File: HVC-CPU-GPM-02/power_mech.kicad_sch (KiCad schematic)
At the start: 19 parts, among them P6 POWER, SW1 RESET, U3 74LS139, U7 74LS368, U8 74LS368

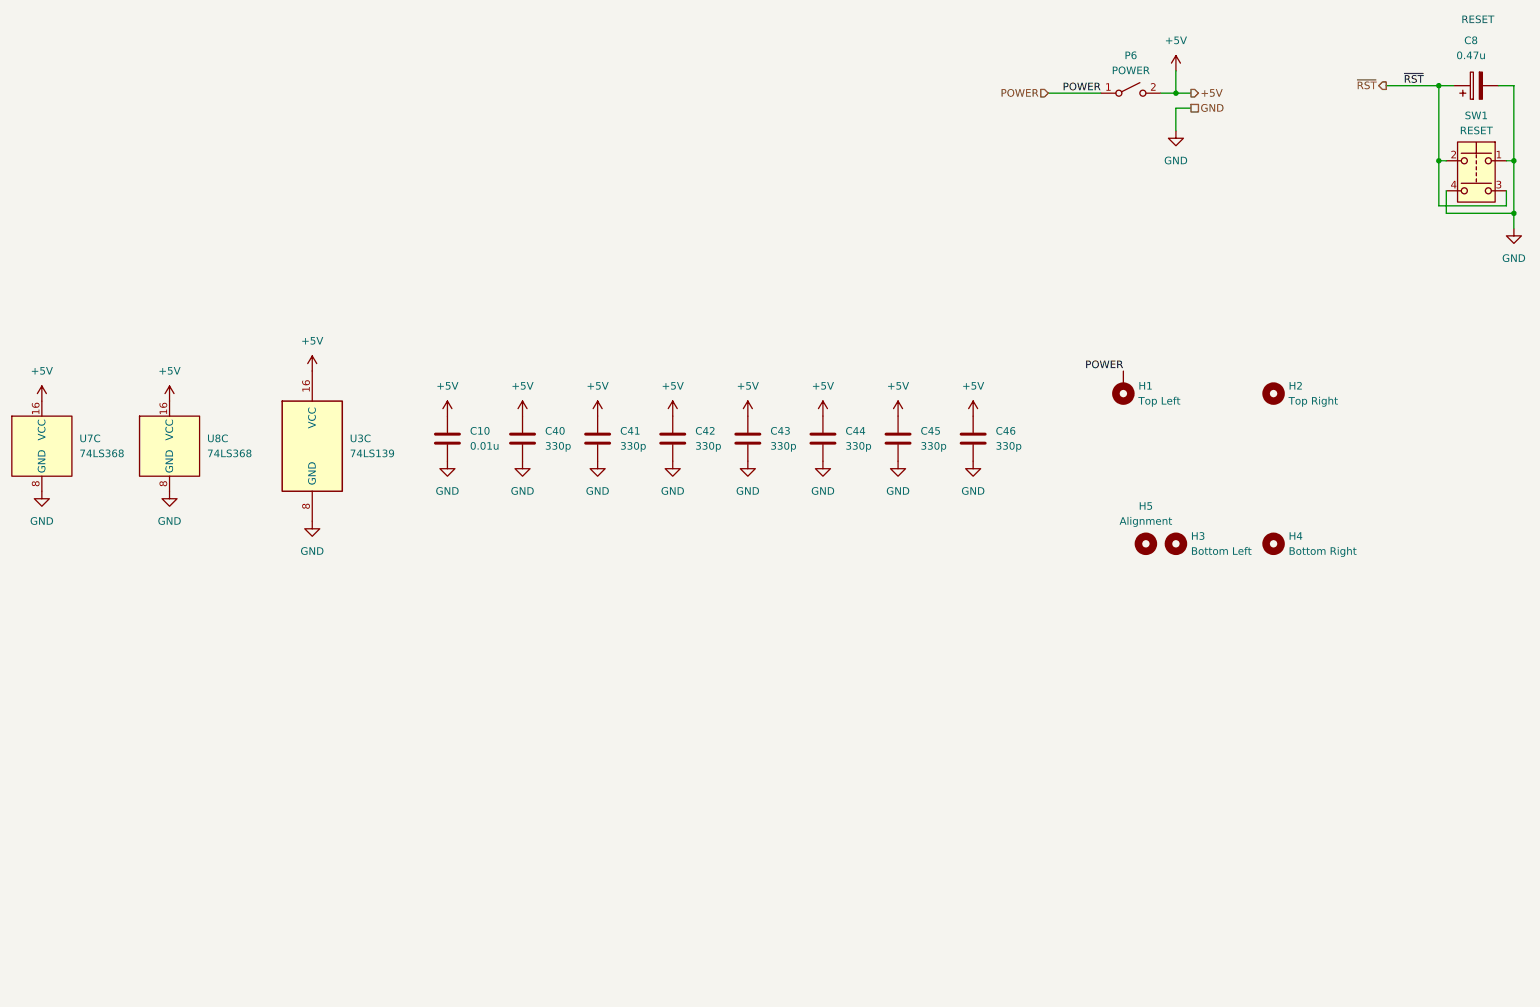
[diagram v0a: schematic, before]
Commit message: Change symbols to functional layout instead of pin map layout Add technical page to store pinouts Organize and compact root page
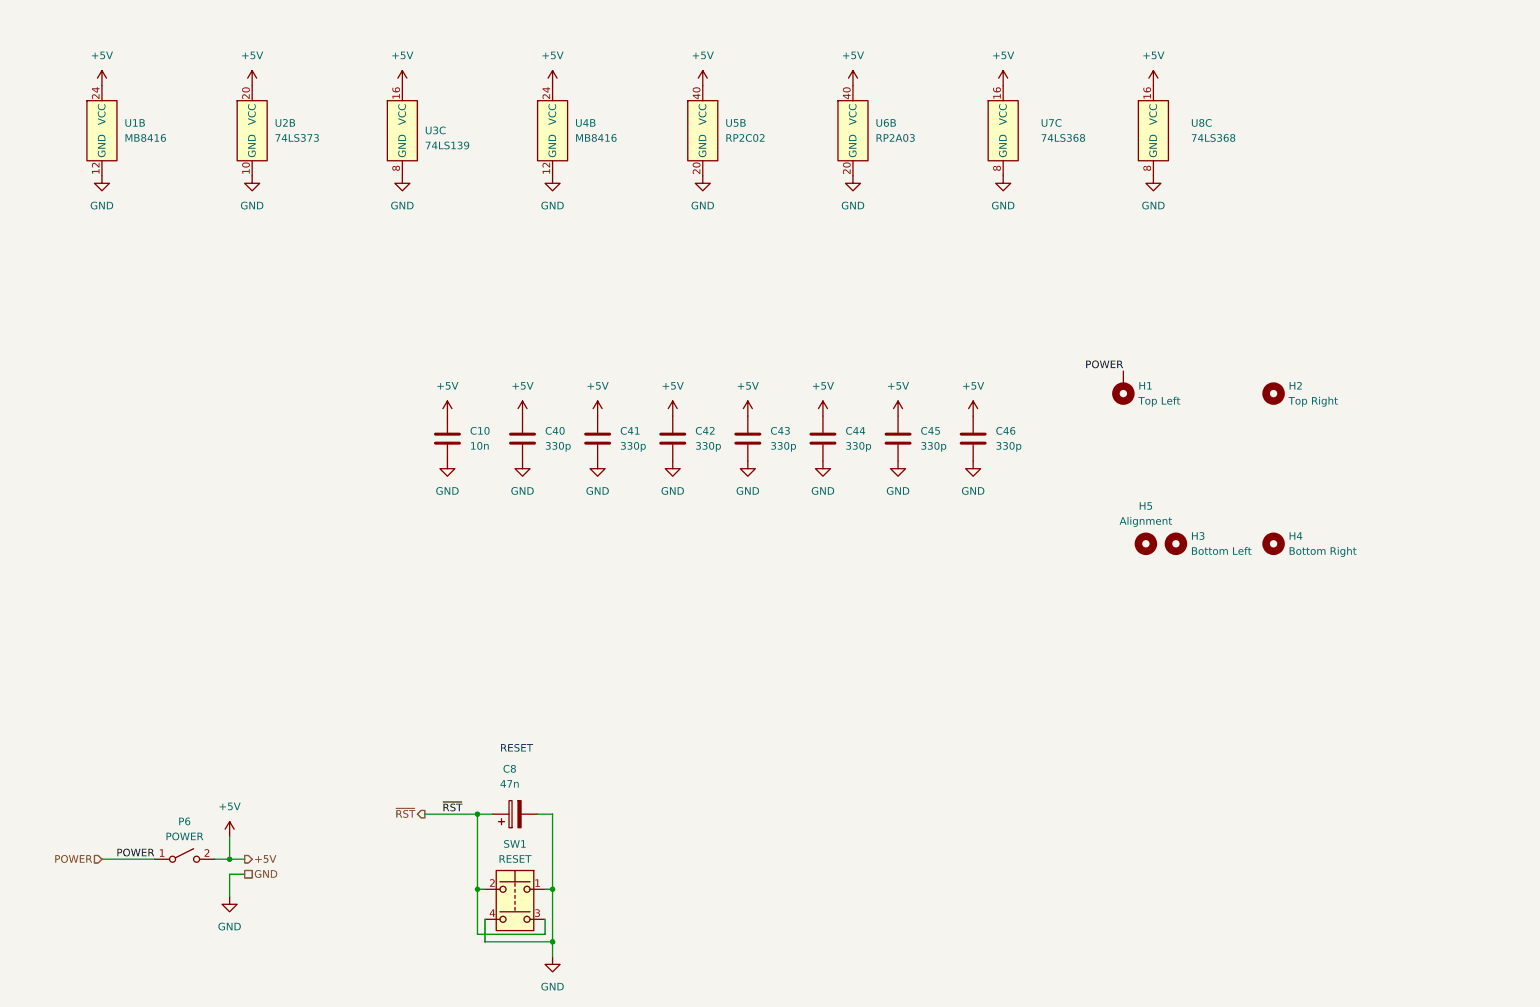
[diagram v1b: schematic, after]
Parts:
- added U1, U4: MB8416, Package_DIP:DIP-24_W7.62mm, symbol Famicom:MB8416
- added U2: 74LS373, Package_DIP:DIP-20_W7.62mm, symbol Famicom:74LS373
- added U5: RP2C02, Package_DIP:DIP-40_W15.24mm, symbol Famicom:RP2C02
- added U6: RP2A03, Package_DIP:DIP-40_W15.24mm, symbol Famicom:RP2A03
- C10: value 0.01u -> 10n
- C8: value 0.47u -> 47n
- U3: symbol 74xx:74LS139 -> Famicom:74LS139
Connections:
- net +5V: now also U1.24 (VCC), U2.20 (VCC), U4.24 (VCC), U5.40 (VCC), U6.40 (VCC)
- net GND: now also U1.12 (GND), U2.10 (GND), U4.12 (GND), U5.20 (GND), U6.20 (GND)
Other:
- moved on the sheet: C8, P6, SW1, U3C, U7C, U8C

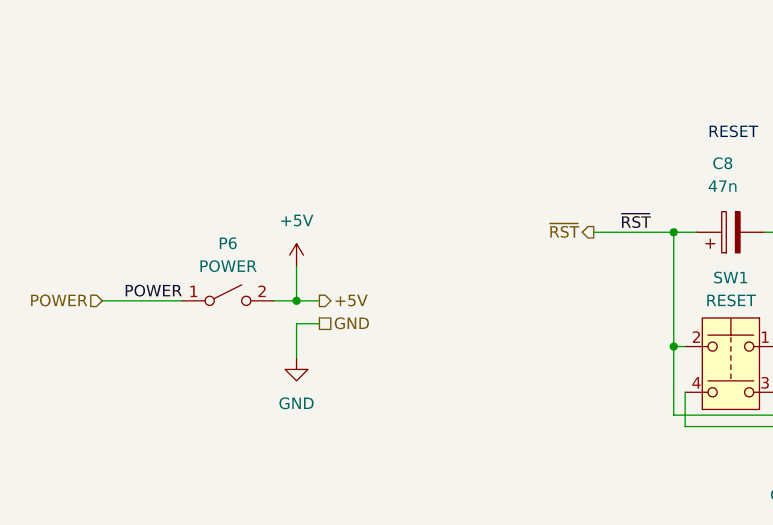
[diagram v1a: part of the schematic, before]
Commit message: Rearranged pins on some symbols to simplify schematic wiring Removed schematics for controller PCBs Added PNG version of schematics
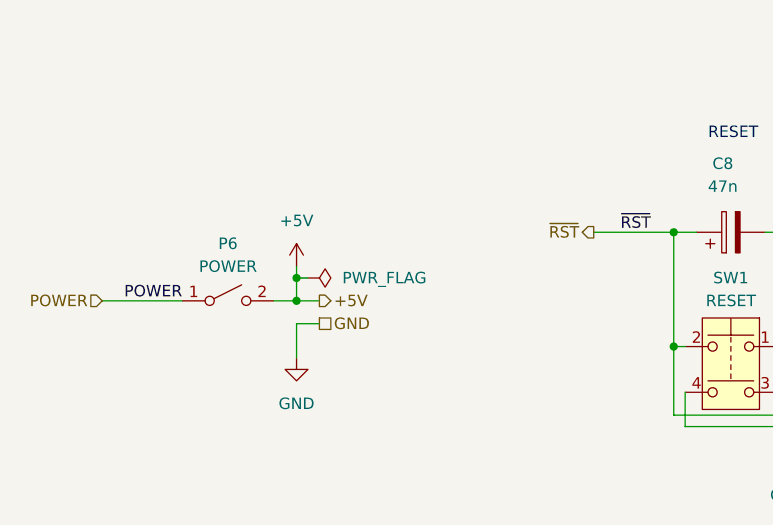
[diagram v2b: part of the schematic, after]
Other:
- title: (none) -> Nintendo Famicom Mainboard
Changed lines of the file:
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@@
 	(generator_version "9.0")
 	(paper "A4")
+	(title_block
+		(title "Nintendo Famicom Mainboard")
+		(date "2025-10-30")
+		(rev "1")
+	)
 	(text "RESET"
 		(exclude_from_sim no)
@@
 		(color 0 0 0 0)
 	)
+	(junction
+		(at 53.34 165.1)
+		(diameter 0)
+		(color 0 0 0 0)
+	)
 	(wire
 		(pts
@@
 	(wire
 		(pts
+			(xy 53.34 165.1) (xy 53.34 163.83)
+		)
+		(stroke
+			(width 0)
+			(type default)
+		)
+	)
+	(wire
+		(pts
 			(xy 53.34 170.18) (xy 53.34 173.99)
 		)
@@
 	(wire
 		(pts
-			(xy 53.34 167.64) (xy 53.34 163.83)
+			(xy 53.34 167.64) (xy 53.34 165.1)
 		)
 		(stroke
@@
 		(pts
 			(xy 107.95 160.02) (xy 107.95 172.72)
+		)
+		(stroke
+			(width 0)
+			(type default)
+		)
+	)
+	(wire
+		(pts
+			(xy 53.34 165.1) (xy 54.61 165.1)
 		)
 		(stroke
@@
 					(unit 1)
 				)
+			)
+		)
+	)
+	(symbol
+		(lib_id "power:PWR_FLAG")
+		(at 54.61 165.1 270)
+		(unit 1)
+		(exclude_from_sim no)
+		(in_bom yes)
+		(on_board yes)
+		(dnp no)
+		(fields_autoplaced yes)
+		(property "Reference" "#FLG01"
+			(at 56.515 165.1 0)
+			(effects
+				(font
+					(size 1.27 1.27)
+				)
+				(hide yes)
+			)
+		)
+		(property "Value" "PWR_FLAG"
+			(at 58.42 165.0999 90)
+			(effects
+				(font
+					(size 1.27 1.27)
+				)
+				(justify left)
+			)
+		)
+		(property "Footprint" ""
+			(at 54.61 165.1 0)
+			(effects
+				(font
+					(size 1.27 1.27)
+				)
+				(hide yes)
+			)
+		)
+		(property "Datasheet" "~"
+			(at 54.61 165.1 0)
+			(effects
+				(font
+					(size 1.27 1.27)
+				)
+				(hide yes)
+			)
+		)
+		(property "Description" "Special symbol for telling ERC where power comes from"
+			(at 54.61 165.1 0)
+			(effects
+				(font
+					(size 1.27 1.27)
+				)
+				(hide yes)
+			)
+		)
+		(pin "1"
+		)
+		(instances
+			(project ""
+				(path "/fb646c2d-03fe-45ba-9ef6-fc3f44aca4b4/26b7c6e0-60f8-49cb-b6c9-8a72e0d0f0d6"
+					(reference "#FLG01")
+					(unit 1)
+				)

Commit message: annotate schematics, correct PCB/schematic parity issure, add datasheets
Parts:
- C10, C40, C41, C42, C43, C44, C45, C46: footprint Nintendo:C_Disc_D3.0mm_W2.0mm_P3.0mm -> Nintendo:C_Disc_NoSilk_D3.0mm_W2.0mm_P3.0mm
- C8: footprint Capacitor_THT:CP_Radial_D5.0mm_P2.50mm -> Nintendo:CP_Radial_D5.0mm_P2.50mm
- U1, U4: footprint Package_DIP:DIP-24_W7.62mm -> Nintendo:DIP-24_W7.62mm
- U2: footprint Package_DIP:DIP-20_W7.62mm -> Nintendo:DIP-20_W7.62mm
- U3, U7, U8: footprint Package_DIP:DIP-16_W7.62mm -> Nintendo:DIP-16_W7.62mm
- U5, U6: footprint Package_DIP:DIP-40_W15.24mm -> Nintendo:DIP-40_W15.24mm
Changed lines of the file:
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@@
 			)
 		)
-		(property "Footprint" "Nintendo:C_Disc_D3.0mm_W2.0mm_P3.0mm"
+		(property "Footprint" "Nintendo:C_Disc_NoSilk_D3.0mm_W2.0mm_P3.0mm"
 			(at 141.9352 100.33 0)
 			(effects
@@
 			)
 		)
-		(property "Footprint" "Nintendo:C_Disc_D3.0mm_W2.0mm_P3.0mm"
+		(property "Footprint" "Nintendo:C_Disc_NoSilk_D3.0mm_W2.0mm_P3.0mm"
 			(at 129.2352 100.33 0)
 			(effects
@@
 			)
 		)
-		(property "Footprint" "Package_DIP:DIP-20_W7.62mm"
+		(property "Footprint" "Nintendo:DIP-20_W7.62mm"
 			(at 57.15 39.37 0)
 			(effects
@@
 			)
 		)
-		(property "Datasheet" "http://www.ti.com/lit/gpn/sn74LS373"
+		(property "Datasheet" "kicad-embed://74LS373.pdf"
 			(at 57.15 39.37 0)
 			(effects
@@
 			)
 		)
-		(property "Footprint" "Nintendo:C_Disc_D3.0mm_W2.0mm_P3.0mm"
+		(property "Footprint" "Nintendo:C_Disc_NoSilk_D3.0mm_W2.0mm_P3.0mm"
 			(at 180.0352 100.33 0)
 			(effects
@@
 			)
 		)
-		(property "Footprint" "Nintendo:C_Disc_D3.0mm_W2.0mm_P3.0mm"
+		(property "Footprint" "Nintendo:C_Disc_NoSilk_D3.0mm_W2.0mm_P3.0mm"
 			(at 103.8352 100.33 0)
 			(effects
@@
 			)
 		)
-		(property "Footprint" "Nintendo:C_Disc_D3.0mm_W2.0mm_P3.0mm"
+		(property "Footprint" "Nintendo:C_Disc_NoSilk_D3.0mm_W2.0mm_P3.0mm"
 			(at 167.3352 100.33 0)
 			(effects
@@
 			)
 		)
-		(property "Footprint" "Package_DIP:DIP-16_W7.62mm"
+		(property "Footprint" "Nintendo:DIP-16_W7.62mm"
 			(at 209.55 39.37 0)
 			(effects
@@
 			)
 		)
-		(property "Datasheet" "http://www.ti.com/lit/gpn/sn74LS368"
+		(property "Datasheet" "kicad-embed://74LS368.pdf"
 			(at 209.55 39.37 0)
 			(effects
@@
 			)
 		)
-		(property "Footprint" "Nintendo:C_Disc_D3.0mm_W2.0mm_P3.0mm"
+		(property "Footprint" "Nintendo:C_Disc_NoSilk_D3.0mm_W2.0mm_P3.0mm"
 			(at 154.6352 100.33 0)
 			(effects
@@
 			)
 		)
-		(property "Footprint" "Package_DIP:DIP-24_W7.62mm"
+		(property "Footprint" "Nintendo:DIP-24_W7.62mm"
 			(at 31.75 39.37 0)
 			(effects
@@
 			)
 		)
-		(property "Datasheet" ""
+		(property "Datasheet" "kicad-embed://MB8416.pdf"
 			(at 31.75 39.37 0)
 			(effects
@@
 			)
 		)
-		(property "Footprint" "Package_DIP:DIP-40_W15.24mm"
+		(property "Footprint" "Nintendo:DIP-40_W15.24mm"
 			(at 133.35 39.37 0)
 			(effects
@@
 			)
 		)
-		(property "Footprint" "Package_DIP:DIP-16_W7.62mm"
+		(property "Footprint" "Nintendo:DIP-16_W7.62mm"
 			(at 184.15 39.37 0)
 			(effects
@@
 			)
 		)
-		(property "Datasheet" "http://www.ti.com/lit/gpn/sn74LS368"
+		(property "Datasheet" "kicad-embed://74LS368.pdf"
 			(at 184.15 39.37 0)
 			(effects
@@
 			)
 		)
-		(property "Footprint" "Nintendo:C_Disc_D3.0mm_W2.0mm_P3.0mm"
+		(property "Footprint" "Nintendo:C_Disc_NoSilk_D3.0mm_W2.0mm_P3.0mm"
 			(at 116.5352 100.33 0)
 			(effects
@@
 			)
 		)
-		(property "Footprint" "Package_DIP:DIP-24_W7.62mm"
+		(property "Footprint" "Nintendo:DIP-24_W7.62mm"
 			(at 107.95 39.37 0)
 			(effects
@@
 			)
 		)
-		(property "Datasheet" ""
+		(property "Datasheet" "kicad-embed://MB8416.pdf"
 			(at 107.95 39.37 0)
 			(effects
@@
 			)
 		)
-		(property "Footprint" "Package_DIP:DIP-40_W15.24mm"
+		(property "Footprint" "Nintendo:DIP-40_W15.24mm"
 			(at 158.75 39.37 0)
 			(effects
@@
 			)
 		)
-		(property "Footprint" "Package_DIP:DIP-16_W7.62mm"
+		(property "Footprint" "Nintendo:DIP-16_W7.62mm"
 			(at 82.55 39.37 0)
 			(effects
@@
 			)
 		)
-		(property "Datasheet" "http://www.ti.com/lit/ds/symlink/sn74ls139a.pdf"
+		(property "Datasheet" "kicad-embed://74LS139.pdf"
 			(at 82.55 39.37 0)
 			(effects
@@
 			)
 		)
-		(property "Footprint" "Nintendo:C_Disc_D3.0mm_W2.0mm_P3.0mm"
+		(property "Footprint" "Nintendo:C_Disc_NoSilk_D3.0mm_W2.0mm_P3.0mm"
 			(at 89.2048 92.71 0)
 			(effects
@@
 			)
 		)
-		(property "Footprint" "Capacitor_THT:CP_Radial_D5.0mm_P2.50mm"
+		(property "Footprint" "Nintendo:CP_Radial_D5.0mm_P2.50mm"
 			(at 105.41 159.0548 0)
 			(effects
